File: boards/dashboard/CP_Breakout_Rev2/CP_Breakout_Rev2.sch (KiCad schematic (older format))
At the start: 17 parts, among them J1 M06LOCK, J2 M02LOCK, J3 M06LOCK, U1 LM2936-3.3, U2 CP2120

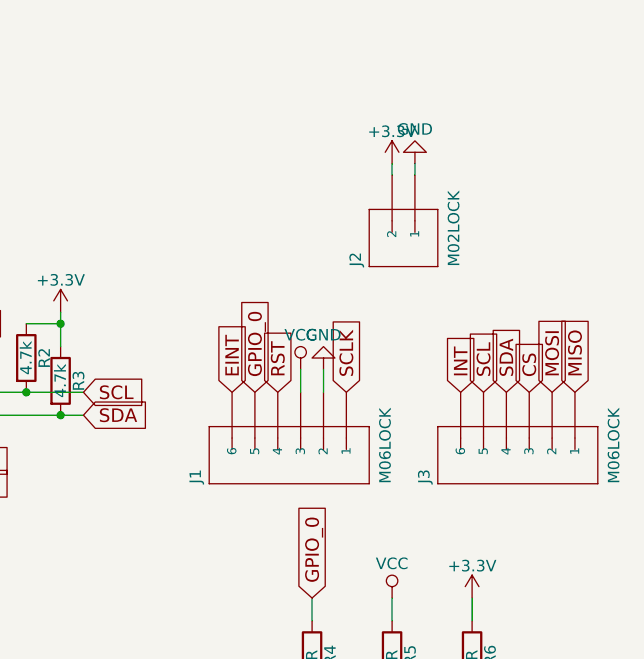
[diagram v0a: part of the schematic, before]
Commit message: Minor changes to CP2120 breakout
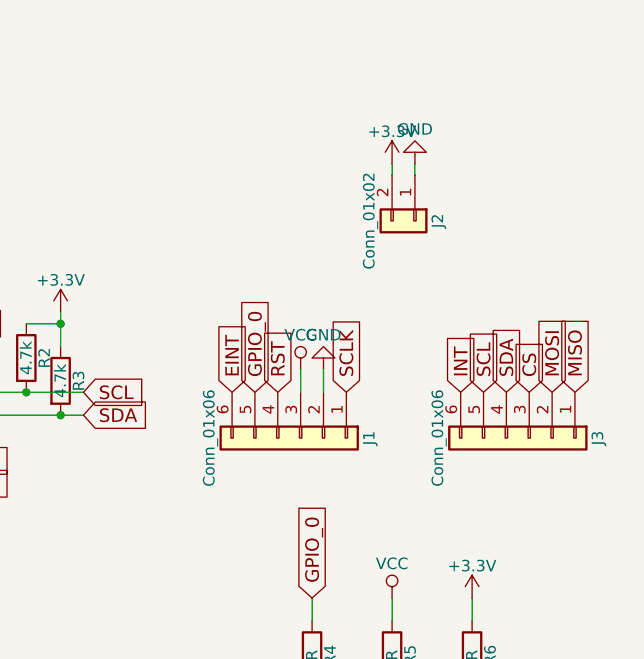
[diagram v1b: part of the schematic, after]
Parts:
- removed J1, J3: M06LOCK, SparkFun-Connectors:1X06_LOCK, symbol M06LOCK
- removed J2: M02LOCK, SparkFun-Connectors:1X02_LOCK, symbol M02LOCK
- added J1, J3: Conn_01x06, Pin_Headers:Pin_Header_Straight_1x06_Pitch2.54mm, symbol Conn_01x06
- added J2: Conn_01x02, Pin_Headers:Pin_Header_Straight_1x02_Pitch2.54mm, symbol Conn_01x02
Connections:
- net +3V3: now also J2.2 (Pin_2)
- net CS: now also J3.3 (Pin_3)
- net EINT: now also J1.6 (Pin_6)
- net GND: now also J1.2 (Pin_2), J2.1 (Pin_1)
- net GPIO_0: now also J1.5 (Pin_5)
- net INT: now also J3.6 (Pin_6)
- net MISO: now also J3.1 (Pin_1)
- net MOSI: now also J3.2 (Pin_2)
- net RST: now also J1.4 (Pin_4)
- net SCL: now also J3.5 (Pin_5)
- net SCLK: now also J1.1 (Pin_1)
- net SDA: now also J3.4 (Pin_4)
- net VCC: now also J1.3 (Pin_3)
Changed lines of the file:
@@
-$EndComp
-$Comp
-L M06LOCK J3
-U 1 1 59F7787C
-P 8600 3850
-F 0 "J3" H 8400 4280 50  0000 L BNN
-F 1 "M06LOCK" H 8400 3450 50  0000 L BNN
-F 2 "SparkFun-Connectors:1X06_LOCK" H 8630 4000 20  0001 C CNN
-F 3 "" H 8600 3850 60  0000 C CNN
-	1    8600 3850
-	0    -1   -1   0
-$EndComp
-$Comp
-L M06LOCK J1
-U 1 1 59F77919
-P 7600 3850
-F 0 "J1" H 7400 4280 50  0000 L BNN
-F 1 "M06LOCK" H 7400 3450 50  0000 L BNN
-F 2 "SparkFun-Connectors:1X06_LOCK" H 7630 4000 20  0001 C CNN
-F 3 "" H 7600 3850 60  0000 C CNN
-	1    7600 3850
-	0    -1   -1   0
 $EndComp
 $Comp
@@
 	4850 3250 4750 3250
 $Comp
-L M02LOCK J2
-U 1 1 59F8B96C
-P 8100 3000
-F 0 "J2" H 8000 3230 50  0000 L BNN
-F 1 "M02LOCK" H 8000 2800 50  0000 L BNN
-F 2 "SparkFun-Connectors:1X02_LOCK" H 8130 3150 20  0001 C CNN
-F 3 "" H 8100 3000 60  0000 C CNN
-	1    8100 3000
-	0    -1   -1   0
+L Conn_01x06 J3
+U 1 1 59FA7CCE
+P 8600 3850
+F 0 "J3" H 8600 4150 50  0000 C CNN
+F 1 "Conn_01x06" H 8600 3450 50  0000 C CNN
+F 2 "Pin_Headers:Pin_Header_Straight_1x06_Pitch2.54mm" H 8600 3850 50  0001 C CNN
+F 3 "" H 8600 3850 50  0001 C CNN
+	1    8600 3850
+	0    1    1    0
+$EndComp
+$Comp
+L Conn_01x06 J1
+U 1 1 59FA7E67
+P 7600 3850
+F 0 "J1" H 7600 4150 50  0000 C CNN
+F 1 "Conn_01x06" H 7600 3450 50  0000 C CNN
+F 2 "Pin_Headers:Pin_Header_Straight_1x06_Pitch2.54mm" H 7600 3850 50  0001 C CNN
+F 3 "" H 7600 3850 50  0001 C CNN
+	1    7600 3850
+	0    1    1    0
+$EndComp
+$Comp
+L Conn_01x02 J2
+U 1 1 59FA82A3
+P 8100 2900
+F 0 "J2" H 8100 3000 50  0000 C CNN
+F 1 "Conn_01x02" H 8100 2700 50  0000 C CNN
+F 2 "Pin_Headers:Pin_Header_Straight_1x02_Pitch2.54mm" H 8100 2900 50  0001 C CNN
+F 3 "" H 8100 2900 50  0001 C CNN
+	1    8100 2900
+	0    1    1    0
 $EndComp
 $EndSCHEMATC

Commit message: Revisions to CP2120 board files
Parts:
- R4, R5, R6: value R -> 500
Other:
- moved on the sheet: D1, D2, D3, J1, J2, J3, R4, R5, R6

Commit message: Progress
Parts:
- removed C3: C_10uF, footprints:C_0805_OEM, symbol C_10uF
- removed R1, R2, R3: 4.7k, footprints:R_0805_OEM, symbol R
- removed R4, R5, R6: 500, footprints:R_0805_OEM, symbol R
- removed U1: LM2936-3.3, SparkFun-PowerIC:SOT223, symbol LM2936-3.3
- added C3: C_0.1uF, footprints:C_0805_OEM, symbol C_0.1uF
- added R1, R2, R3: 4.7kR, footprints:R_0805_OEM, symbol 4.7kR
- added R4, R5, R6: R_499, footprints:R_0805_OEM, symbol R_499
- added U1: LM3480, TO_SOT_Packages_SMD:SOT-23, symbol LM3480
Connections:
- net +3V3: now also C3.1, R1.1, R2.1, R3.1, R6.1, U1.1 (VO)
- net GND: now also C3.2, U1.3 (GND)
- net GPIO_0: now also R4.1
- net RST: now also R1.2
- net SCL: now also R2.2
- net SDA: now also R3.2
- net VCC: now also R5.1, U1.2 (VI)
- net at D1.2 (A): now also R4.2
- net at D2.2 (A): now also R5.2
- net at D3.2 (A): now also R6.2
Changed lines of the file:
@@
-$EndComp
-$Comp
-L C_10uF C3
-U 1 1 59F77735
-P 4600 2300
-F 0 "C3" H 4625 2400 50  0000 L CNN
-F 1 "C_10uF" H 4625 2200 50  0000 L CNN
-F 2 "footprints:C_0805_OEM" H 4638 2150 50  0001 C CNN
-F 3 "http://datasheets.avx.com/cx5r.pdf" H 4625 2400 50  0001 C CNN
-F 4 "478-5167-1-ND" H 4600 2300 60  0001 C CNN "MPN"
-F 5 "Digi-Key" H 4600 2300 60  0001 C CNN "MFN"
-F 6 "Value" H 4600 2300 60  0001 C CNN "Package"
-F 7 "https://www.digikey.com/product-detail/en/avx-corporation/0805ZD106KAT2A/478-5167-1-ND/1913257" H 5025 2800 60  0001 C CNN "PurchasingLink"
-	1    4600 2300
-	1    0    0    -1
 $EndComp
 $Comp
@@
 $EndComp
 $Comp
-L R R4
-U 1 1 59F779A0
-P 7750 2800
-F 0 "R4" V 7830 2800 50  0000 C CNN
-F 1 "500" V 7750 2800 50  0000 C CNN
-F 2 "footprints:R_0805_OEM" V 7680 2800 50  0001 C CNN
-F 3 "" H 7750 2800 50  0001 C CNN
-	1    7750 2800
-	1    0    0    -1
-$EndComp
-$Comp
-L R R5
-U 1 1 59F779F2
-P 8100 2800
-F 0 "R5" V 8180 2800 50  0000 C CNN
-F 1 "500" V 8100 2800 50  0000 C CNN
-F 2 "footprints:R_0805_OEM" V 8030 2800 50  0001 C CNN
-F 3 "" H 8100 2800 50  0001 C CNN
-	1    8100 2800
-	1    0    0    -1
-$EndComp
-$Comp
 L C_0.1uF C2
 U 1 1 59F77A32
@@
 $EndComp
 $Comp
-L R R6
-U 1 1 59F77AF7
-P 8450 2800
-F 0 "R6" V 8530 2800 50  0000 C CNN
-F 1 "500" V 8450 2800 50  0000 C CNN
-F 2 "footprints:R_0805_OEM" V 8380 2800 50  0001 C CNN
-F 3 "" H 8450 2800 50  0001 C CNN
-	1    8450 2800
-	1    0    0    -1
-$EndComp
-$Comp
 L +3.3V #PWR01
 U 1 1 59F78D77
@@
 F 3 "" H 5400 4450 50  0001 C CNN
 	1    5400 4450
-	1    0    0    -1
-$EndComp
-$Comp
-L R R2
-U 1 1 59F7C7FD
-P 6400 3500
-F 0 "R2" V 6480 3500 50  0000 C CNN
-F 1 "4.7k" V 6400 3500 50  0000 C CNN
-F 2 "footprints:R_0805_OEM" V 6330 3500 50  0001 C CNN
-F 3 "" H 6400 3500 50  0001 C CNN
-	1    6400 3500
-	1    0    0    -1
-$EndComp
-$Comp
-L R R3
-U 1 1 59F7C8CA
-P 6550 3600
-F 0 "R3" V 6630 3600 50  0000 C CNN
-F 1 "4.7k" V 6550 3600 50  0000 C CNN
-F 2 "footprints:R_0805_OEM" V 6480 3600 50  0001 C CNN
-F 3 "" H 6550 3600 50  0001 C CNN
-	1    6550 3600
 	1    0    0    -1
 $EndComp
@@
 Wire Wire Line
 	6650 2250 6650 2200
-$Comp
-L R R1
-U 1 1 59F7EB19
-P 4050 3300
-F 0 "R1" V 4130 3300 50  0000 C CNN
-F 1 "4.7k" V 4050 3300 50  0000 C CNN
-F 2 "footprints:R_0805_OEM" V 3980 3300 50  0001 C CNN
-F 3 "" H 4050 3300 50  0001 C CNN
-	1    4050 3300
-	1    0    0    -1
-$EndComp
 Wire Wire Line
 	4350 3350 4350 3650
@@
 Wire Wire Line
 	4050 3150 4050 3100
-$Comp
-L LM2936-3.3 U1
-U 1 1 59F8B32B
-P 4150 2150
-F 0 "U1" H 4000 2275 50  0000 C CNN
-F 1 "LM2936-3.3" H 4150 2275 50  0000 L CNN
-F 2 "SparkFun-PowerIC:SOT223" H 4150 2375 50  0001 C CIN
-F 3 "" H 4150 2100 50  0001 C CNN
-	1    4150 2150
-	1    0    0    -1
-$EndComp
 Wire Wire Line
 	4450 2150 4850 2150
@@
 	0    1    1    0
 $EndComp
+$Comp
+L LM3480 U1
+U 1 1 5A0E50F5
+P 4150 2150
+F 0 "U1" H 4000 2275 50  0000 C CNN
+F 1 "LM3480" H 4150 2275 50  0000 L CNN
+F 2 "TO_SOT_Packages_SMD:SOT-23" H 4100 2350 50  0001 C CNN
+F 3 "" H 4250 1900 50  0001 C CNN
+	1    4150 2150
+	1    0    0    -1
+$EndComp
+$Comp
+L C_0.1uF C3
+U 1 1 5A0E5198
+P 4600 2300
+F 0 "C3" H 4625 2400 50  0000 L CNN
+F 1 "C_0.1uF" H 4625 2200 50  0000 L CNN
+F 2 "footprints:C_0805_OEM" H 4638 2150 50  0001 C CNN
+F 3 "http://datasheets.avx.com/X7RDielectric.pdf" H 4625 2400 50  0001 C CNN
+F 4 "478-3352-1-ND" H 4600 2300 60  0001 C CNN "MPN"
+F 5 "Digi-Key" H 4600 2300 60  0001 C CNN "MFN"
+F 6 "Value" H 4600 2300 60  0001 C CNN "Package"
+F 7 "https://www.digikey.com/products/en?keywords=478-3352-1-ND" H 5025 2800 60  0001 C CNN "PurchasingLink"
+	1    4600 2300
+	1    0    0    -1
+$EndComp
+$Comp
+L 4.7kR R1
+U 1 1 5A1338FF
+P 4050 3300
+F 0 "R1" V 4130 3300 50  0000 C CNN
+F 1 "4.7kR" V 3950 3300 50  0000 C CNN
+F 2 "footprints:R_0805_OEM" V 3980 3300 50  0001 C CNN
+F 3 "" H 4050 3300 50  0001 C CNN
+	1    4050 3300
+	1    0    0    -1
+$EndComp
+$Comp
+L 4.7kR R2
+U 1 1 5A133A30
+P 6400 3500
+F 0 "R2" V 6480 3500 50  0000 C CNN
+F 1 "4.7kR" V 6300 3500 50  0000 C CNN
+F 2 "footprints:R_0805_OEM" V 6330 3500 50  0001 C CNN
+F 3 "" H 6400 3500 50  0001 C CNN
+	1    6400 3500
+	1    0    0    -1
+$EndComp
+$Comp
+L 4.7kR R3
+U 1 1 5A133AB8
+P 6550 3600
+F 0 "R3" V 6630 3600 50  0000 C CNN
+F 1 "4.7kR" V 6450 3600 50  0000 C CNN
+F 2 "footprints:R_0805_OEM" V 6480 3600 50  0001 C CNN
+F 3 "" H 6550 3600 50  0001 C CNN
+	1    6550 3600
+	1    0    0    -1
+$EndComp
+$Comp
+L R_499 R4
+U 1 1 5A14858B
+P 7750 2800
+F 0 "R4" V 7830 2800 50  0000 C CNN
+F 1 "R_499" V 7650 2800 50  0000 C CNN
+F 2 "footprints:R_0805_OEM" H 7680 2800 50  0001 C CNN
+F 3 "http://www.yageo.com.tw/exep/pages/download/literatures/PYu-R_INT-thick_7.pdf" H 7830 2800 50  0001 C CNN
+F 4 "Digi-Key" H 7750 2800 60  0001 C CNN "MFN"
+F 5 "RC0805FR-07499RL" H 7750 2800 60  0001 C CNN "MPN"
+F 6 "Value" H 7750 2800 60  0001 C CNN "Package"
+F 7 "https://www.digikey.com/product-detail/en/yageo/RC0805FR-07499RL/311-499CRCT-ND/730933" H 8230 3200 60  0001 C CNN "PurchasingLink"
+	1    7750 2800
+	1    0    0    -1
+$EndComp
+$Comp
+L R_499 R5
+U 1 1 5A1486C3
+P 8100 2800
+F 0 "R5" V 8180 2800 50  0000 C CNN
+F 1 "R_499" V 8000 2800 50  0000 C CNN
+F 2 "footprints:R_0805_OEM" H 8030 2800 50  0001 C CNN
+F 3 "http://www.yageo.com.tw/exep/pages/download/literatures/PYu-R_INT-thick_7.pdf" H 8180 2800 50  0001 C CNN
+F 4 "Digi-Key" H 8100 2800 60  0001 C CNN "MFN"
+F 5 "RC0805FR-07499RL" H 8100 2800 60  0001 C CNN "MPN"
+F 6 "Value" H 8100 2800 60  0001 C CNN "Package"
+F 7 "https://www.digikey.com/product-detail/en/yageo/RC0805FR-07499RL/311-499CRCT-ND/730933" H 8580 3200 60  0001 C CNN "PurchasingLink"
+	1    8100 2800
+	1    0    0    -1
+$EndComp
+$Comp
+L R_499 R6
+U 1 1 5A148719
+P 8450 2800
+F 0 "R6" V 8530 2800 50  0000 C CNN
+F 1 "R_499" V 8350 2800 50  0000 C CNN
+F 2 "footprints:R_0805_OEM" H 8380 2800 50  0001 C CNN
+F 3 "http://www.yageo.com.tw/exep/pages/download/literatures/PYu-R_INT-thick_7.pdf" H 8530 2800 50  0001 C CNN
+F 4 "Digi-Key" H 8450 2800 60  0001 C CNN "MFN"
+F 5 "RC0805FR-07499RL" H 8450 2800 60  0001 C CNN "MPN"
+F 6 "Value" H 8450 2800 60  0001 C CNN "Package"
+F 7 "https://www.digikey.com/product-detail/en/yageo/RC0805FR-07499RL/311-499CRCT-ND/730933" H 8930 3200 60  0001 C CNN "PurchasingLink"
+	1    8450 2800
+	1    0    0    -1
+$EndComp
 $EndSCHEMATC
